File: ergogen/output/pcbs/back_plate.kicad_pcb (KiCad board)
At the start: 2 copper layers, 144.2 x 91.9 mm, 6 parts

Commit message: new shape
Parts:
- removed ?: , solar_system
- moved MH4 15.9 mm to (104.5, 92.8), turned to 10 degrees
- moved MH3 15.6 mm to (143.4, 98.1), turned to -15 degrees
- moved MH2 6.89 mm to (127.1, 46.3)
- moved MH5 5.62 mm to (73.6, 78.6)
- moved MH1 2.52 mm to (90.5, 47.3)
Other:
- board size 144.2 x 91.9 mm -> 147.1 x 107.2 mm

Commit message: update generated files
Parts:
- moved MH3 20.0 mm to (160.6, 108.1), turned to -30 degrees
- moved MH4 19.6 mm to (124.1, 92.9), turned to 0 degrees
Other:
- outline, holes or cut-outs redrawn
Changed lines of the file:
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@@
   (title_block
     (title "back_plate")
-    (date "2025-11-10")
+    (date "2025-11-12")
     (rev "1")
     (company "curtis bollinger")
@@
   (footprint "ceoloide:mounting_hole_npth"
     (layer "F.Cu")
-    (at 143.3735818 98.05513279999998 -15)
+    (at 160.64669740000002 108.05669409999999 -30)
     (property "Reference" "MH3"
-      (at 0 2.55 -15)
-      (layer "F.SilkS")
-      hide
-      (effects (font (size 1 1) (thickness 0.15)))
-    )
-    (pad "" np_thru_hole circle
-      (at 0 0 -15)
-      (size 2.2 2.2)
-      (drill 2.2)
-      (layers "*.Cu" "*.Mask")
-    )
-  )
-  (footprint "ceoloide:mounting_hole_npth"
-    (layer "F.Cu")
-    (at 104.4990997 92.84759689999998 10)
+      (at 0 2.55 -30)
+      (layer "F.SilkS")
+      hide
+      (effects (font (size 1 1) (thickness 0.15)))
+    )
+    (pad "" np_thru_hole circle
+      (at 0 0 -30)
+      (size 2.2 2.2)
+      (drill 2.2)
+      (layers "*.Cu" "*.Mask")
+    )
+  )
+  (footprint "ceoloide:mounting_hole_npth"
+    (layer "F.Cu")
+    (at 124.10043890000001 92.86497739999999 0)
     (property "Reference" "MH4"
-      (at 0 2.55 10)
-      (layer "F.SilkS")
-      hide
-      (effects (font (size 1 1) (thickness 0.15)))
-    )
-    (pad "" np_thru_hole circle
-      (at 0 0 10)
+      (at 0 2.55 0)
+      (layer "F.SilkS")
+      hide
+      (effects (font (size 1 1) (thickness 0.15)))
+    )
+    (pad "" np_thru_hole circle
+      (at 0 0 0)
       (size 2.2 2.2)
       (drill 2.2)
@@
 (gr_circle (center 90.4816205 47.33459739999999) (end 91.5816205 47.33459739999999) (layer Edge.Cuts) (stroke (width 0.15) (type default)) (fill none))
 (gr_circle (center 127.12162050000002 46.33459739999999) (end 128.22162050000003 46.33459739999999) (layer Edge.Cuts) (stroke (width 0.15) (type default)) (fill none))
-(gr_circle (center 143.3735818 98.05513279999998) (end 144.4735818 98.05513279999998) (layer Edge.Cuts) (stroke (width 0.15) (type default)) (fill none))
-(gr_circle (center 104.4990997 92.84759689999998) (end 105.5990997 92.84759689999998) (layer Edge.Cuts) (stroke (width 0.15) (type default)) (fill none))
+(gr_circle (center 160.64669740000002 108.05669409999999) (end 161.74669740000002 108.05669409999999) (layer Edge.Cuts) (stroke (width 0.15) (type default)) (fill none))
+(gr_circle (center 124.10043890000001 92.86497739999999) (end 125.20043890000001 92.86497739999999) (layer Edge.Cuts) (stroke (width 0.15) (type default)) (fill none))
 (gr_circle (center 73.55589330000001 78.6000269) (end 74.6558933 78.6000269) (layer Edge.Cuts) (stroke (width 0.15) (type default)) (fill none))
 )

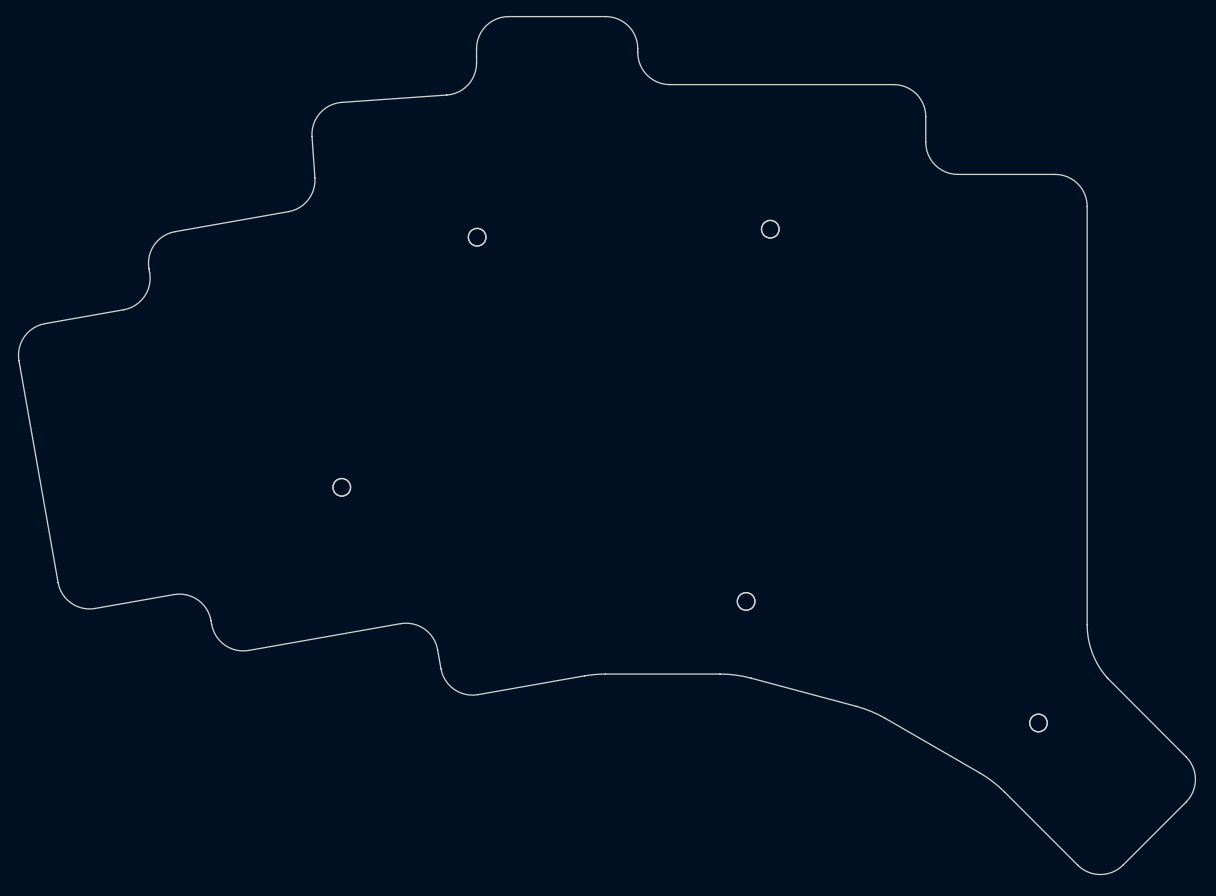
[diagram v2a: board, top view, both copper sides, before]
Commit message: working on new case
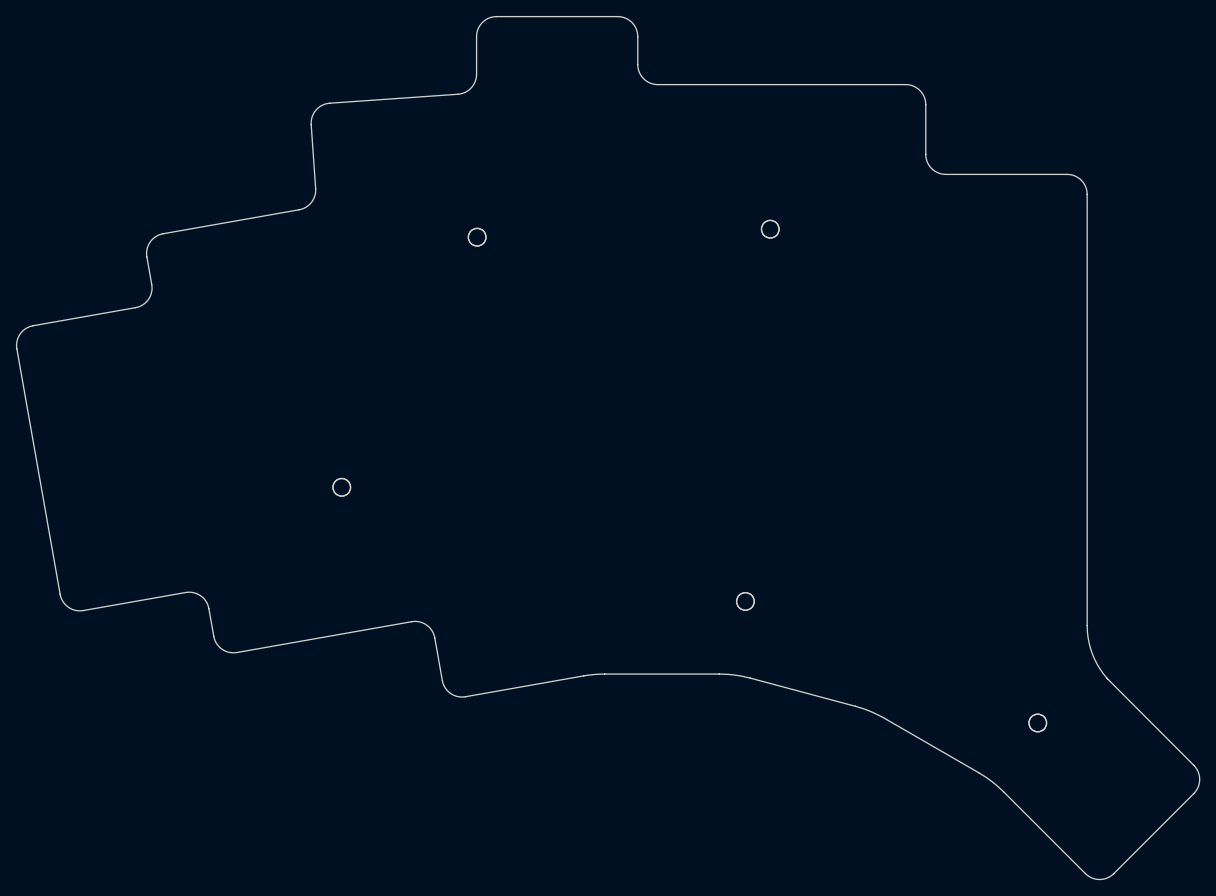
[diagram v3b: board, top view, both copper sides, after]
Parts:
- moved MH4 0.09 mm to (124.0, 92.9)
- moved MH3 0.09 mm to (160.6, 108.1)
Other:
- board size 147.1 x 107.2 mm -> 147.9 x 107.9 mm
